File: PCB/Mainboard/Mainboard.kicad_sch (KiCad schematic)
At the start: 5 parts, among them J6 Conn_GPS, Q1 AO3400A, U1 ESP32-DEVKIT-V1, U2 ESP32-DEVKIT-V1, U3 WIFI_KIT_32__V3_

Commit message: First rev is done
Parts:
- added BT1: BK-18650-PC8, Felix:BAT_BK-18650-PC8, symbol Felix:BK-18650-PC8
- added H1, H2, H3, H4: MountingHole_Pad, MountingHole:MountingHole_3.2mm_M3_Pad, symbol Mechanical:MountingHole_Pad
- added JP1, JP2, JP3: SolderJumper_3_Open, Jumper:SolderJumper-3_P2.0mm_Open_TrianglePad1.0x1.5mm_NumberLabels, symbol Jumper:SolderJumper_3_Open
- added JP10, JP11, JP4, JP5, JP6, JP9: SolderJumper_2_Open, Jumper:SolderJumper-2_P1.3mm_Open_TrianglePad1.0x1.5mm, symbol Jumper:SolderJumper_2_Open
- J6: value Conn_GPS -> GPS
- U1, U2: footprint Felix:MODULE_ESP32_DEVKIT_V1 -> Felix:MODULE_ESP32_DEVKIT_V1_NO_WIFI
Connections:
- net +3.3V: no longer U1.1 (3V3)
- net ADS1115/A1: now also JP3.2 (C)
- net ADS1115/A2: now also JP1.2 (C)
- net ADS1115/A3: now also JP2.2 (C)
- net ADS1115/SCL: now also U2.26 (D14); no longer U2.3 (D15)
- net ADS1115/SDA: now also U2.27 (D12); no longer U2.9 (D18)
- net GND: now also BT1.4-, H1.1, H2.1, H3.1, H4.1, JP4.2 (B), JP5.2 (B), JP6.2 (B)
- net SdCard/CS: now also U2.19 (D34); no longer U2.8 (D5)
- net SdCard/MISO: now also U2.22 (D33); no longer U2.27 (D12)
- net SdCard/MOSI: now also U2.21 (D32); no longer U2.28 (D13)
- net SdCard/SCK: now also U2.20 (D35); no longer U2.26 (D14)
- net GsmModule/RST: now reaches U1.14 (D22)
- net GsmModule/SLEEP: now reaches U1.15 (D23)
- net GsmModule/TX: now reaches U1.6 (RX2)
- net GsmModule/RX: now reaches U1.7 (TX2)
- net at U3.J2_14 (GPIO5/ADC1_CH4/TOUCH5): now also U2.6 (RX2)
- net at U3.J2_15 (GPIO4/ADC1_CH3/TOUCH4): now also U2.7 (TX2)
- new net: BT1.2+, JP1.1 (A), JP10.2 (B), JP2.3 (B), JP9.1 (A)
- new net: BT1.3+, JP1.3 (B), JP10.1 (A), JP11.2 (B), JP3.1 (A)
- new net: BT1.1+, JP2.1 (A), JP9.2 (B)
- new net: BT1.2-, JP5.1 (A)
- new net: BT1.1-, JP4.1 (A)
- new net: BT1.3-, JP6.1 (A)
- new net +3V8: BT1.4+, JP11.1 (A), JP3.3 (B)
- new net GPSModule/VCC: U1.1 (3V3)
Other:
- added sheet GsmModule (GsmModule.kicad_sch)
- sheet GPSModule ports: added VCC; removed none
- sheet GPSModule1 ports: added VCC; removed none
- moved on the sheet: U1, U3B

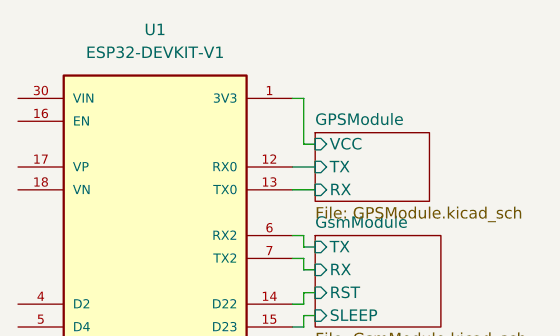
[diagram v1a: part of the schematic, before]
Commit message: rouned the corners
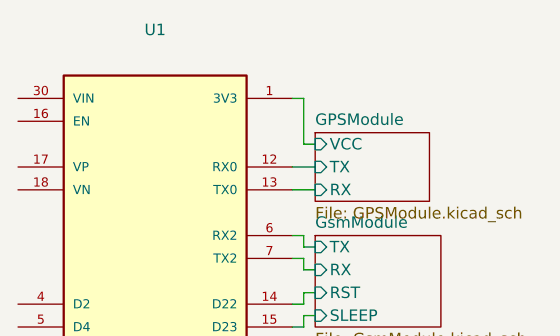
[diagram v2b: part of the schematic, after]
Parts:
- U1, U2: footprint Felix:MODULE_ESP32_DEVKIT_V1_NO_WIFI -> Felix:MODULE_ESP32_DEVKIT_V1_NO_WIFI_No_Hole
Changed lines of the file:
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@@
 					(size 1.27 1.27)
 				)
-			)
-		)
-		(property "Footprint" "Felix:MODULE_ESP32_DEVKIT_V1_NO_WIFI"
+				(hide yes)
+			)
+		)
+		(property "Footprint" "Felix:MODULE_ESP32_DEVKIT_V1_NO_WIFI_No_Hole"
 			(at 34.29 50.8 0)
 			(effects
@@
 			)
 		)
-		(property "Footprint" "Felix:MODULE_ESP32_DEVKIT_V1_NO_WIFI"
+		(property "Footprint" "Felix:MODULE_ESP32_DEVKIT_V1_NO_WIFI_No_Hole"
 			(at 105.41 127 0)
 			(effects

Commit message: updated some resitor values
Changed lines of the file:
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@@
 (kicad_sch
-	(version 20231120)
+	(version 20250114)
 	(generator "eeschema")
-	(generator_version "8.0")
+	(generator_version "9.0")
 	(paper "A4")
 	(junction
@@
 	(label "RX"
 		(at 186.69 99.06 0)
-		(fields_autoplaced yes)
 		(effects
 			(font
@@
 	(label "TX"
 		(at 189.23 99.06 0)
-		(fields_autoplaced yes)
 		(effects
 			(font
@@
 		(at 132.08 135.89)
 		(size 12.7 10.16)
+		(exclude_from_sim no)
+		(in_bom yes)
+		(on_board yes)
+		(dnp no)
 		(fields_autoplaced yes)
 		(stroke
@@
 		(at 38.1 96.52)
 		(size 12.7 10.16)
+		(exclude_from_sim no)
+		(in_bom yes)
+		(on_board yes)
+		(dnp no)
 		(fields_autoplaced yes)
 		(stroke
@@
 		(at 53.34 138.43)
 		(size 12.7 10.16)
+		(exclude_from_sim no)
+		(in_bom yes)
+		(on_board yes)
+		(dnp no)
 		(fields_autoplaced yes)
 		(stroke
@@
 		(at 123.19 105.41)
 		(size 12.7 7.62)
+		(exclude_from_sim no)
+		(in_bom yes)
+		(on_board yes)
+		(dnp no)
 		(fields_autoplaced yes)
 		(stroke
@@
 		(at 52.07 40.64)
 		(size 13.97 10.16)
+		(exclude_from_sim no)
+		(in_bom yes)
+		(on_board yes)
+		(dnp no)
 		(fields_autoplaced yes)
 		(stroke
@@
 		(at 24.13 138.43)
 		(size 12.7 3.81)
+		(exclude_from_sim no)
+		(in_bom yes)
+		(on_board yes)
+		(dnp no)
 		(fields_autoplaced yes)
 		(stroke
@@
 		(at 52.07 29.21)
 		(size 12.7 7.62)
+		(exclude_from_sim no)
+		(in_bom yes)
+		(on_board yes)
+		(dnp no)
 		(fields_autoplaced yes)
 		(stroke
@@
 		)
 	)
+	(embedded_fonts no)
 )
